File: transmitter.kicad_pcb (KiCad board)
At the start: 2 copper layers, 200 x 200 mm, 242 parts, among them IC1 W9864G6KH-6, IC2 TPS61165DBVR, IC3 MT25QL128ABA1ESE-0SIT, IC4 USBLC6-2SC6, J1 AFC01-S40FCA-00, J2 AFC07-S10ECC-00, J3 B2B-PH-K-S, J4 B2B-PH-K-S, J5 B3B-PH-K-S, J6 USB4085-GF-A, J7 Conn_01x05, J9 Conn_02x06_Odd_Even, Q1 AO3400A, Q2 AO3400A, Q3 SI2301CDS-T1-GE3, Q4 AO3400A, SW1 Button SPST SMD Tactile Switch, SW2 Button SPST SMD Tactile Switch, SW3 Button SPST SMD Tactile Switch, SW4 Button SPST SMD Tactile Switch, SW5 Button SPST SMD Tactile Switch, SW6 Button SPST SMD Tactile Switch, SW7 SW_SPDT_MSM, SW8 Button SPST SMD Tactile Switch, SW9 RotaryEncoder_Switch, U1 STM32H743ZIT6TR, U2 CAT24C256, U3 MP2667GG-0000-Z, U4 AMS1117-3.3, U5 TPS61252DSG, U6 PCA9554APW, Y1 32.768KHZ, Y2 X322525MOB4SI-25MHz

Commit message: example new layout
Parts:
- moved R16 301.5 mm to (28.5, 68.3), turned to 90 degrees
- moved R17 299.8 mm to (30.4, 68.3), turned to 90 degrees
- moved C23 294.5 mm to (36.4, 68.3), turned to 90 degrees
- moved C24 292.8 mm to (38.4, 68.3), turned to 90 degrees
- moved RV1 290.8 mm to (30.2, 76.7), turned to 90 degrees
- moved RV2 284.9 mm to (36.7, 76.7), turned to 90 degrees
- moved C40 284.8 mm to (50.5, 33.7)
- moved C43 284.8 mm to (57.0, 33.2)
- moved R51 284.8 mm to (54.1, 33.2)
- moved R52 284.8 mm to (54.1, 35.2)
- moved IC4 284.8 mm to (45.6, 34.5)
- moved S2 273.7 mm to (24.7, 26.6), turned to -90 degrees
- moved R34 273.4 mm to (29.6, 31.0)
- moved R35 273.4 mm to (29.6, 33.0)
- moved C34 267.9 mm to (24.5, 33.5)
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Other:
- board size 200 x 200 mm -> 200 x 110 mm

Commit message: change to 6layer
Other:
- copper layers 2 -> 6
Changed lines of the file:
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@@
 	(layers
 		(0 "F.Cu" signal)
+		(4 "In1.Cu" signal)
+		(6 "In2.Cu" signal)
+		(8 "In3.Cu" signal)
+		(10 "In4.Cu" signal)
 		(2 "B.Cu" signal)
 		(9 "F.Adhes" user "F.Adhesive")
@@
 	)
 	(setup
+		(stackup
+			(layer "F.SilkS"
+				(type "Top Silk Screen")
+			)
+			(layer "F.Paste"
+				(type "Top Solder Paste")
+			)
+			(layer "F.Mask"
+				(type "Top Solder Mask")
+				(thickness 0.01)
+			)
+			(layer "F.Cu"
+				(type "copper")
+				(thickness 0.035)
+			)
+			(layer "dielectric 1"
+				(type "prepreg")
+				(thickness 0.1)
+				(material "FR4")
+				(epsilon_r 4.5)
+				(loss_tangent 0.02)
+			)
+			(layer "In1.Cu"
+				(type "copper")
+				(thickness 0.035)
+			)
+			(layer "dielectric 2"
+				(type "core")
+				(thickness 0.535)
+				(material "FR4")
+				(epsilon_r 4.5)
+				(loss_tangent 0.02)
+			)
+			(layer "In2.Cu"
+				(type "copper")
+				(thickness 0.035)
+			)
+			(layer "dielectric 3"
+				(type "prepreg")
+				(thickness 0.1)
+				(material "FR4")
+				(epsilon_r 4.5)
+				(loss_tangent 0.02)
+			)
+			(layer "In3.Cu"
+				(type "copper")
+				(thickness 0.035)
+			)
+			(layer "dielectric 4"
+				(type "core")
+				(thickness 0.535)
+				(material "FR4")
+				(epsilon_r 4.5)
+				(loss_tangent 0.02)
+			)
+			(layer "In4.Cu"
+				(type "copper")
+				(thickness 0.035)
+			)
+			(layer "dielectric 5"
+				(type "prepreg")
+				(thickness 0.1)
+				(material "FR4")
+				(epsilon_r 4.5)
+				(loss_tangent 0.02)
+			)
+			(layer "B.Cu"
+				(type "copper")
+				(thickness 0.035)
+			)
+			(layer "B.Mask"
+				(type "Bottom Solder Mask")
+				(thickness 0.01)
+			)
+			(layer "B.Paste"
+				(type "Bottom Solder Paste")
+			)
+			(layer "B.SilkS"
+				(type "Bottom Silk Screen")
+			)
+			(copper_finish "None")
+			(dielectric_constraints no)
+		)
 		(pad_to_mask_clearance 0)
 		(allow_soldermask_bridges_in_footprints no)

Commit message: very very prototype layout + routing sdram
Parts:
- removed JP2: NC, Jumper:SolderJumper-2_P1.3mm_Open_TrianglePad1.0x1.5mm
- added C86: 100nF, 0_capacitors:C_0402_1005Metric, F.Cu at (172.6, 75.5)
- added C87: 100nF, 0_capacitors:C_0402_1005Metric, F.Cu at (172.6, 80.3)
- added R95: 0Ω, 0_resistors:R_0402_1005Metric, F.Cu at (150.4, 73.5)
- moved C82 117.0 mm to (189.0, 105.8), turned to 180 degrees
- moved C84 116.6 mm to (187.5, 112.1), turned to 180 degrees
- moved C81 115.8 mm to (189.0, 100.5)
- moved C83 115.3 mm to (187.4, 106.9), turned to 180 degrees
- moved R80 114.3 mm to (185.2, 110.0)
- moved R81 112.9 mm to (185.2, 108.9)
- moved R83 109.5 mm to (185.1, 103.3)
- moved R82 109.4 mm to (185.1, 102.1)
- moved R92 66.0 mm to (147.1, 94.5)
- moved R93 65.6 mm to (147.1, 95.7)
- moved R94 62.3 mm to (144.4, 95.7)
- moved IC3 59.7 mm to (105.7, 67.5), turned to 90 degrees
- moved IC1 56.2 mm to (164.9, 81.9)
- moved C22 54.5 mm to (109.7, 80.3)
- moved R15 54.5 mm to (106.8, 80.3)
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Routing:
- net /Project Architecture/MCU - IO/FMC_D15: track 0.00 -> 78.7 mm
- net /Project Architecture/MCU - IO/FMC_D14: track 0.00 -> 78.7 mm
- net /Project Architecture/MCU - IO/FMC_D13: track 0.00 -> 77.7 mm
- net /Project Architecture/MCU - IO/FMC_D10: track 0.00 -> 63.0 mm
- net /Project Architecture/MCU - IO/FMC_D8: track 0.00 -> 62.8 mm
- net /Project Architecture/MCU - IO/FMC_D9: track 0.00 -> 62.8 mm
- net /Project Architecture/MCU - IO/FMC_D12: track 0.00 -> 62.7 mm
- net /Project Architecture/MCU - IO/FMC_D11: track 0.00 -> 62.7 mm
- net /Project Architecture/MCU - IO/FMC_A11: track 0.00 -> 59.6 mm
- net /Project Architecture/MCU - IO/FMC_A10: track 0.00 -> 58.9 mm, vias 0 -> 2
- net /Project Architecture/MCU - IO/FMC_D7: track 0.00 -> 58.0 mm, vias 0 -> 2
- net /Project Architecture/MCU - IO/FMC_A9: track 0.00 -> 57.1 mm
- net /Project Architecture/MCU - IO/FMC_A8: track 0.00 -> 56.6 mm
- net /Project Architecture/MCU - IO/FMC_A7: track 0.00 -> 56.0 mm
- net /Project Architecture/MCU - IO/FMC_A6: track 0.00 -> 53.8 mm
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
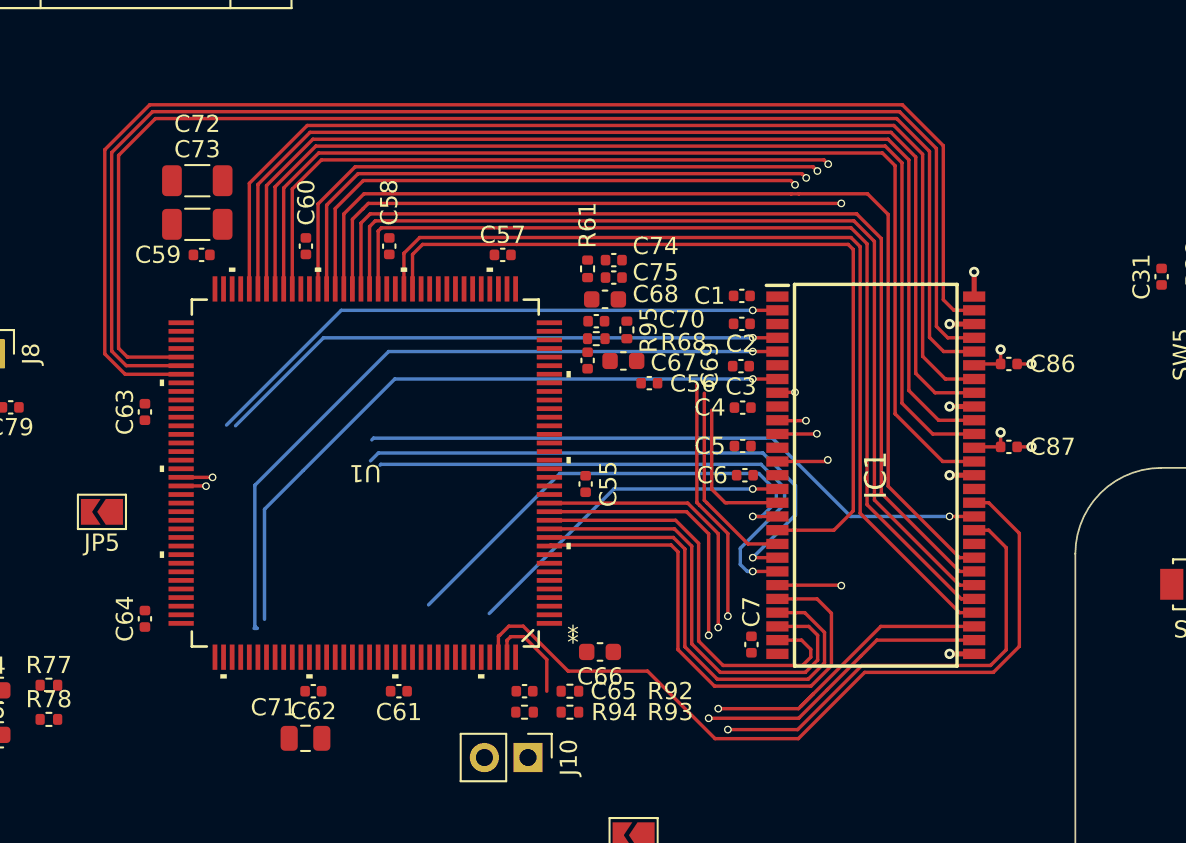
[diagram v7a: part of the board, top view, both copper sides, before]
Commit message: slightly new layout and sdram routing
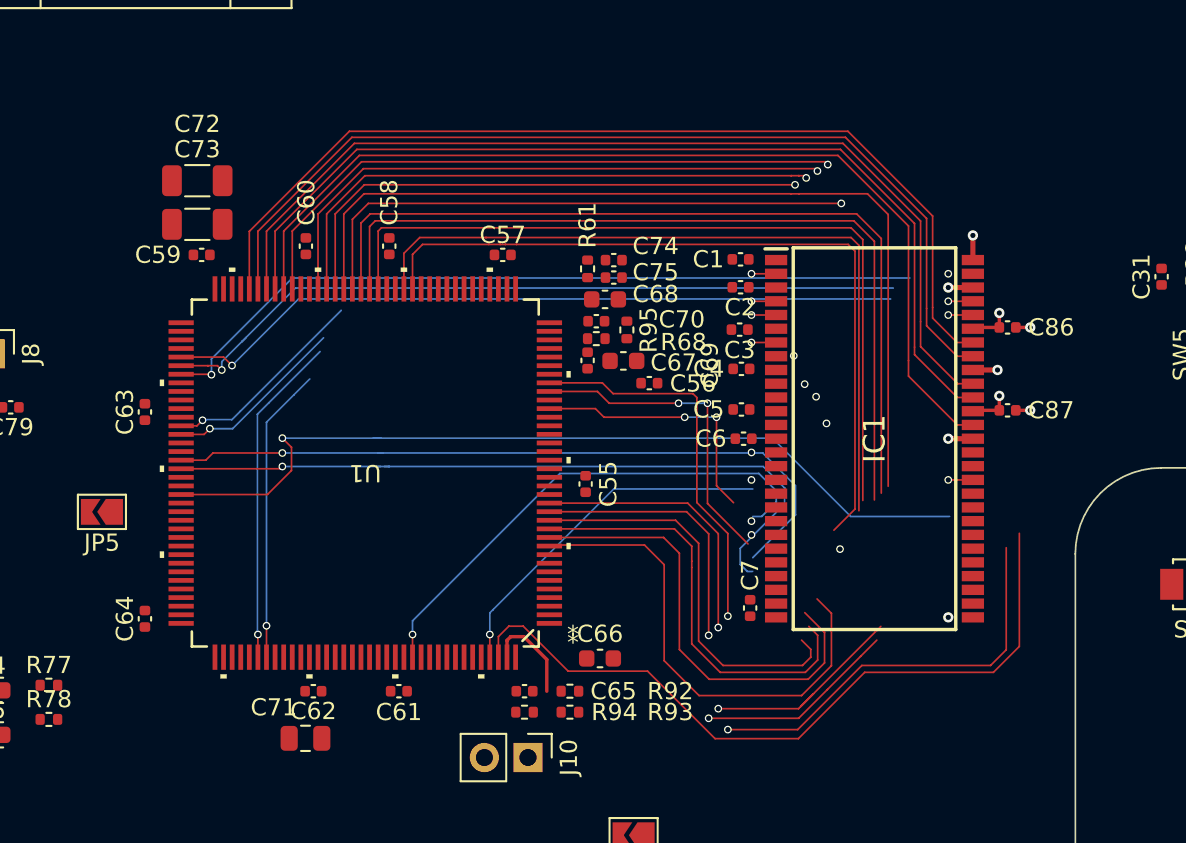
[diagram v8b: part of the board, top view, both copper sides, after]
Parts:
- moved C4 2.26 mm to (157.1, 75.7)
- moved C6 2.13 mm to (157.2, 79.8)
- moved C7 2.13 mm to (157.6, 89.7)
- moved IC1 2.13 mm to (164.8, 79.8)
- moved C2 2.13 mm to (157.0, 71.0)
- moved C86 2.13 mm to (172.6, 73.3)
- moved C3 2.13 mm to (157.0, 73.5)
- moved C1 2.13 mm to (157.0, 69.4)
- moved C5 2.13 mm to (157.1, 78.1)
- moved C87 2.13 mm to (172.6, 78.1)
- moved C66 0.38 mm to (148.8, 92.6), turned to 0 degrees
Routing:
- net /Project Architecture/MCU - IO/FMC_D15: track 78.7 -> 45.3 mm, vias 0 -> 2
- net /Project Architecture/MCU - IO/FMC_D13: track 77.7 -> 44.5 mm, vias 0 -> 2
- net /Project Architecture/MCU - IO/FMC_D14: track 78.7 -> 45.6 mm, vias 0 -> 2
- net /Project Architecture/MCU - IO/FMC_D1: track 33.7 -> 12.1 mm, vias 1 -> 2
- net /Project Architecture/MCU - IO/FMC_D2: track 42.2 -> 20.7 mm, vias 1 -> 2
- net /Project Architecture/MCU - IO/FMC_D0: track 34.8 -> 13.5 mm, vias 1 -> 2
- net /Project Architecture/MCU - IO/FMC_D3: track 39.4 -> 18.7 mm, vias 1 -> 2
- net /Project Architecture/MCU - IO/FMC_D5: track 49.5 -> 33.3 mm
- net /Project Architecture/MCU - IO/FMC_SDCLK: track 37.0 -> 51.7 mm, vias 1 -> 2
- net /Project Architecture/MCU - IO/FMC_BA1: track 32.0 -> 42.6 mm, vias 1 -> 2
- net /Project Architecture/MCU - IO/FMC_BA0: track 32.4 -> 42.2 mm, vias 1 -> 3
- net /Project Architecture/MCU - IO/FMC_A6: track 53.8 -> 44.6 mm
- net /Project Architecture/MCU - IO/FMC_A7: track 56.0 -> 47.1 mm
- net /Project Architecture/MCU - IO/FMC_A8: track 56.6 -> 48.7 mm
- net /Project Architecture/MCU - IO/FMC_A9: track 57.1 -> 49.8 mm
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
